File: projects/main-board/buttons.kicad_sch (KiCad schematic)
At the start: 16 parts, among them SW10 SW_Push, SW11 SW_Push, SW12 SW_Push, SW13 SW_Push, SW14 SW_Push, SW15 SW_Push, SW16 SW_Push, SW17 SW_Push, SW2 SW_Push, SW3 SW_Push, SW4 SW_Push, SW5 SW_Push, SW6 SW_Push, SW7 SW_Push, SW8 SW_Push, SW9 SW_Push

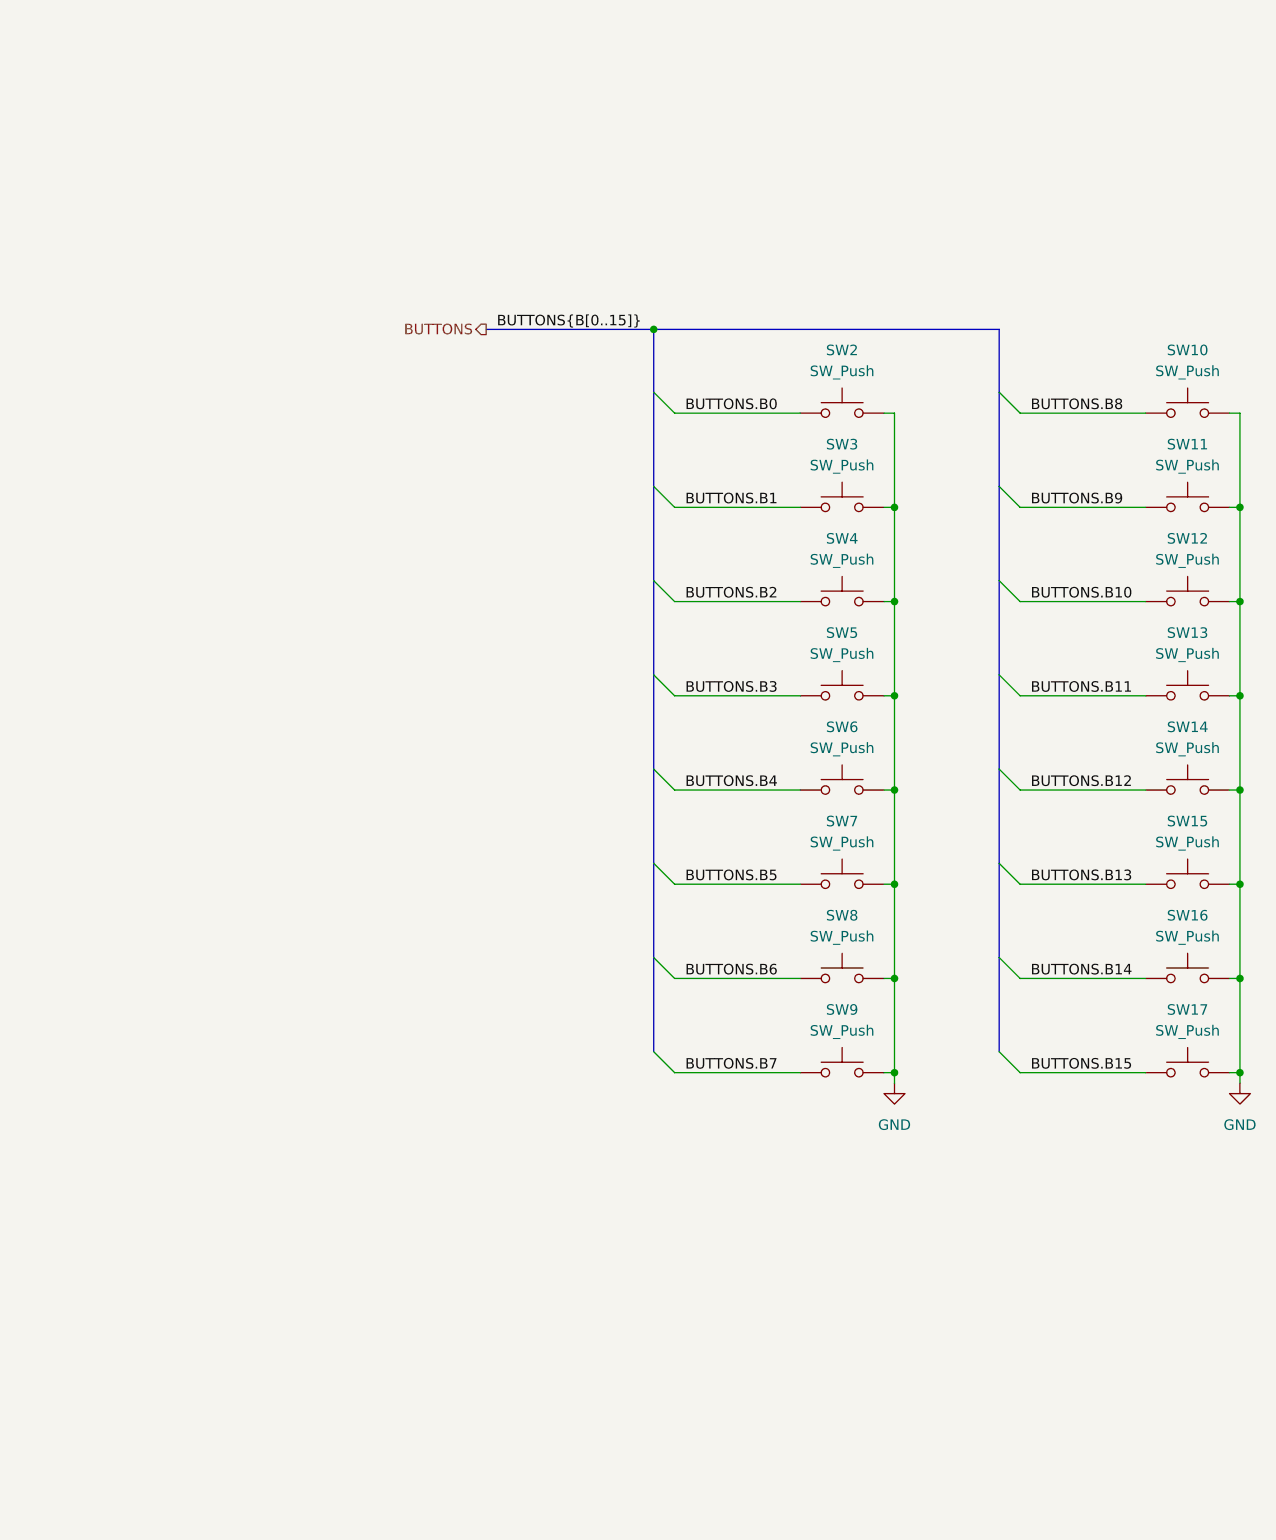
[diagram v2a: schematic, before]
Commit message: Add footprints
- Inductors
- Switches
- Buttons
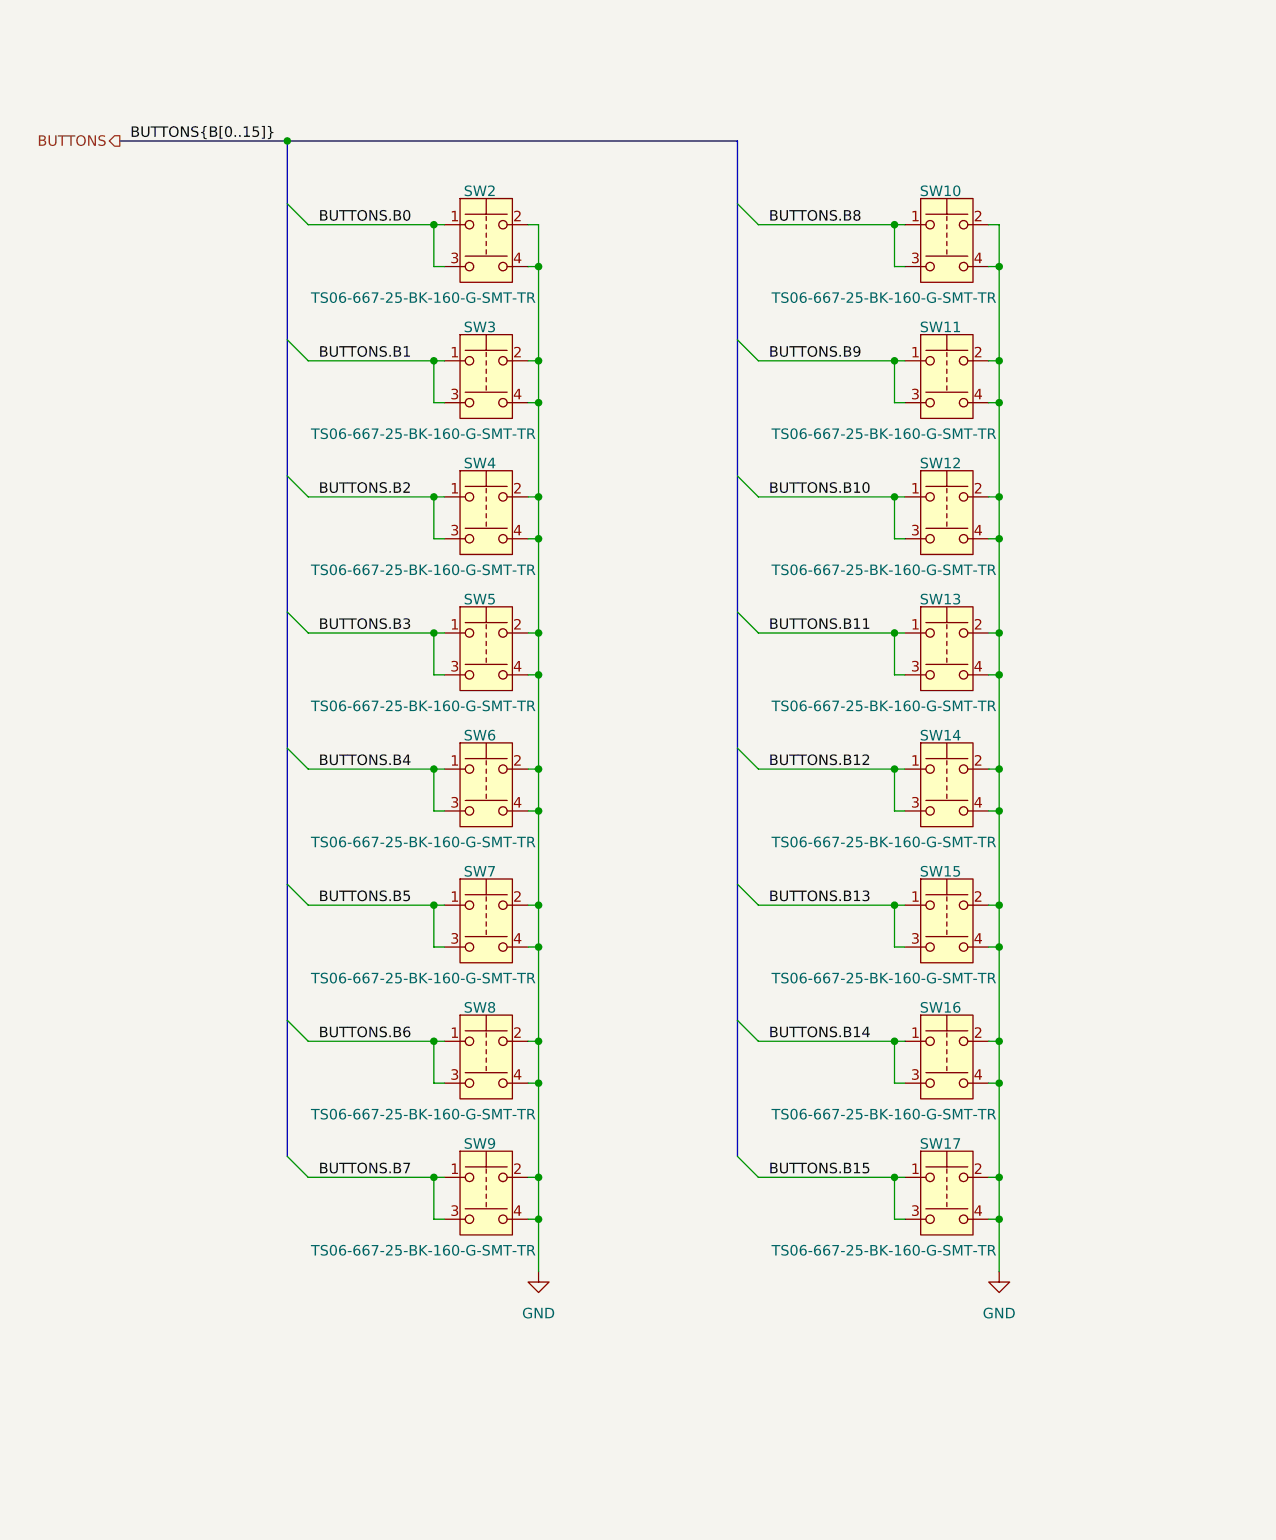
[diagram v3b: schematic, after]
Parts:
- removed SW10, SW11, SW12, SW13, SW14, SW15, SW16, SW17, SW2, SW3, SW4, SW5, SW6, SW7, SW8, SW9: SW_Push, symbol Switch:SW_Push
- added SW10, SW11, SW12, SW13, SW14, SW15, SW16, SW17, SW2, SW3, SW4, SW5, SW6, SW7, SW8, SW9: TS06-667-25-BK-160-G-SMT-TR, footprint-library:TS06-667-25-BK-160-G-SMT-TR, symbol symbol-library:TS06-667-25-BK-160-G-SMT-TR
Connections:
- net BUTTONS.B0: now also SW2.1, SW2.3
- net BUTTONS.B1: now also SW3.1, SW3.3
- net BUTTONS.B10: now also SW12.1, SW12.3
- net BUTTONS.B11: now also SW13.1, SW13.3
- net BUTTONS.B12: now also SW14.1, SW14.3
- net BUTTONS.B13: now also SW15.1, SW15.3
- net BUTTONS.B14: now also SW16.1, SW16.3
- net BUTTONS.B15: now also SW17.1, SW17.3
- net BUTTONS.B2: now also SW4.1, SW4.3
- net BUTTONS.B3: now also SW5.1, SW5.3
- net BUTTONS.B4: now also SW6.1, SW6.3
- net BUTTONS.B5: now also SW7.1, SW7.3
- net BUTTONS.B6: now also SW8.1, SW8.3
- net BUTTONS.B7: now also SW9.1, SW9.3
- net BUTTONS.B8: now also SW10.1, SW10.3
- net BUTTONS.B9: now also SW11.1, SW11.3
- net GND: now also SW10.2, SW10.4, SW11.2, SW11.4, SW12.2, SW12.4, SW13.2, SW13.4, SW14.2, SW14.4, SW15.2, SW15.4, SW16.2, SW16.4, SW17.2, SW17.4, SW2.2, SW2.4, SW3.2, SW3.4, SW4.2, SW4.4, SW5.2, SW5.4, SW6.2, SW6.4, SW7.2, SW7.4, SW8.2, SW8.4, SW9.2, SW9.4

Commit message: Fix footprint DRC errors.
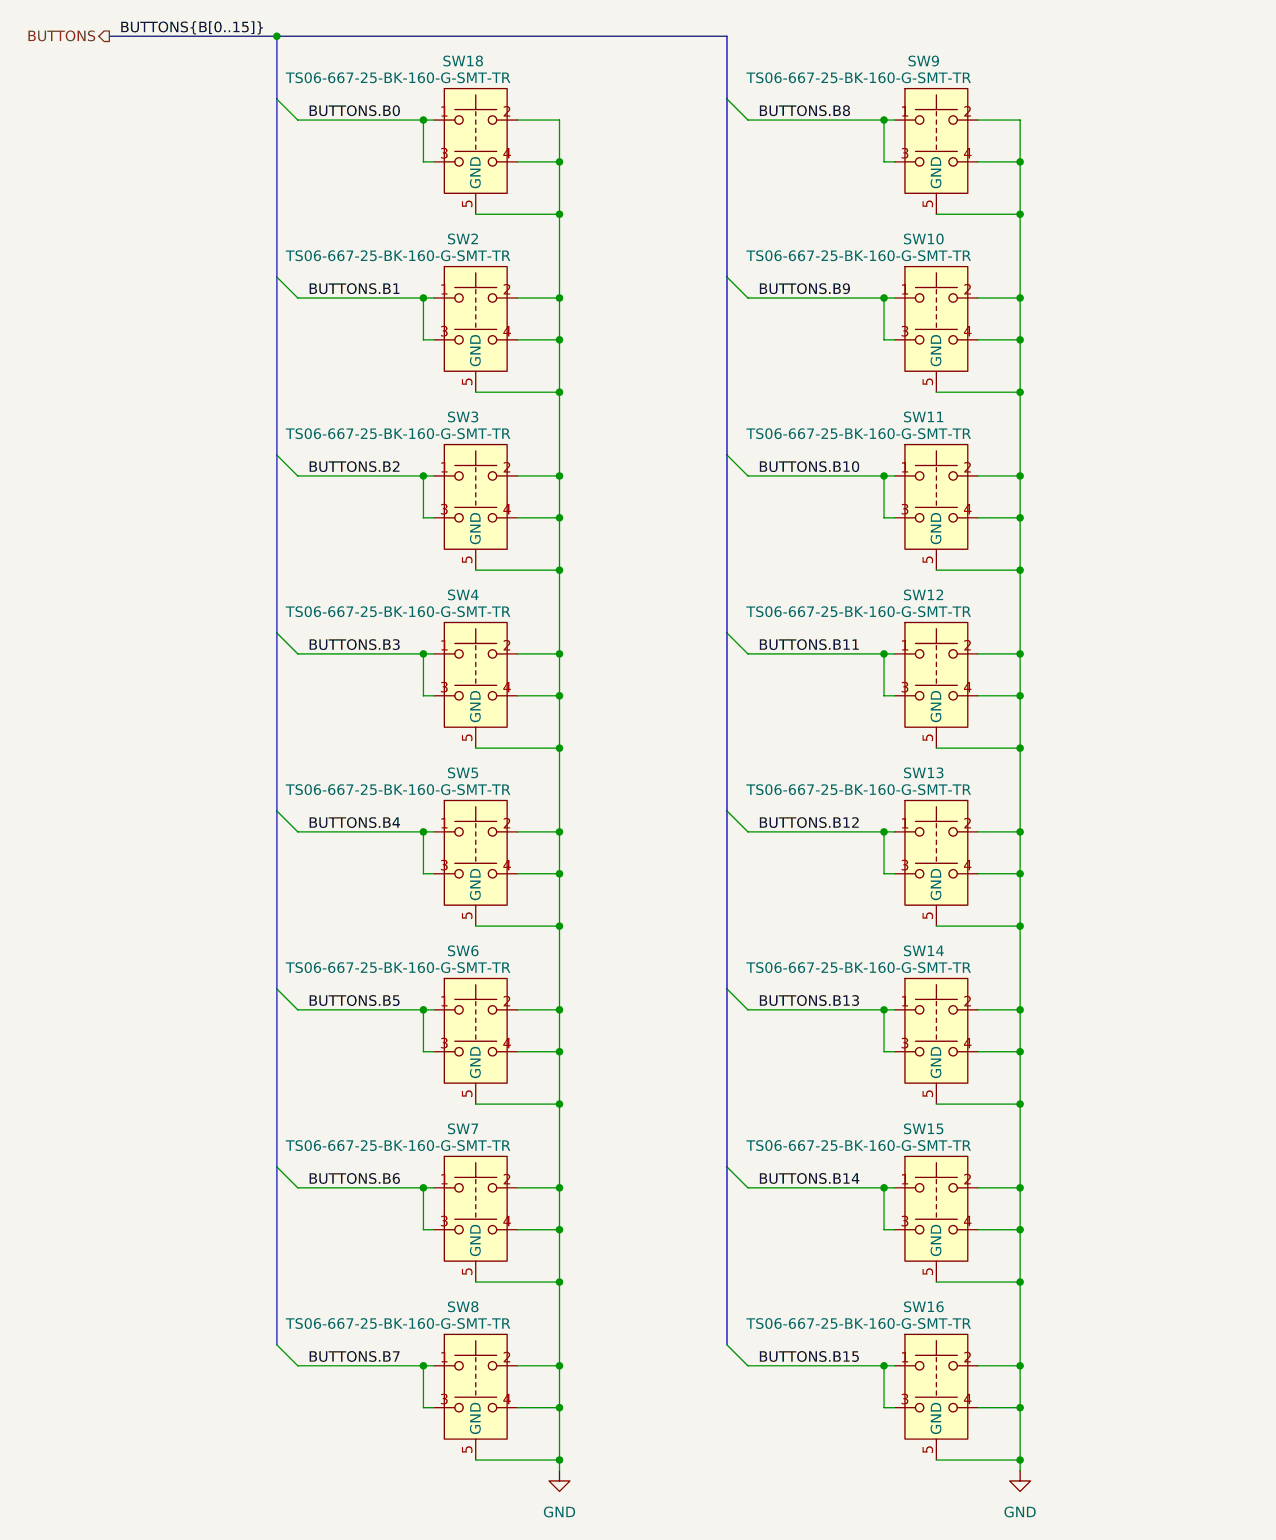
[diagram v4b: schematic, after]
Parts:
- removed SW17: TS06-667-25-BK-160-G-SMT-TR, footprint-library:TS06-667-25-BK-160-G-SMT-TR, symbol symbol-library:TS06-667-25-BK-160-G-SMT-TR
- added SW18: TS06-667-25-BK-160-G-SMT-TR, footprint-library:TS06-667-25-BK-160-G-SMT-TR, symbol symbol-library:TS06-667-25-BK-160-G-SMT-TR
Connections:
- net BUTTONS.B0: now also SW18.1, SW18.3; no longer SW2.1, SW2.3
- net BUTTONS.B1: now also SW2.1, SW2.3; no longer SW3.1, SW3.3
- net BUTTONS.B10: now also SW11.1, SW11.3; no longer SW12.1, SW12.3
- net BUTTONS.B11: now also SW12.1, SW12.3; no longer SW13.1, SW13.3
- net BUTTONS.B12: now also SW13.1, SW13.3; no longer SW14.1, SW14.3
- net BUTTONS.B13: now also SW14.1, SW14.3; no longer SW15.1, SW15.3
- net BUTTONS.B14: now also SW15.1, SW15.3; no longer SW16.1, SW16.3
- net BUTTONS.B15: now also SW16.1, SW16.3
- net BUTTONS.B2: now also SW3.1, SW3.3; no longer SW4.1, SW4.3
- net BUTTONS.B3: now also SW4.1, SW4.3; no longer SW5.1, SW5.3
- net BUTTONS.B4: now also SW5.1, SW5.3; no longer SW6.1, SW6.3
- net BUTTONS.B5: now also SW6.1, SW6.3; no longer SW7.1, SW7.3
- net BUTTONS.B6: now also SW7.1, SW7.3; no longer SW8.1, SW8.3
- net BUTTONS.B7: now also SW8.1, SW8.3; no longer SW9.1, SW9.3
- net BUTTONS.B8: now also SW9.1, SW9.3; no longer SW10.1, SW10.3
- net BUTTONS.B9: now also SW10.1, SW10.3; no longer SW11.1, SW11.3
- net GND: now also SW10.5 (GND), SW11.5 (GND), SW12.5 (GND), SW13.5 (GND), SW14.5 (GND), SW15.5 (GND), SW16.5 (GND), SW2.5 (GND), SW3.5 (GND), SW4.5 (GND), SW5.5 (GND), SW6.5 (GND), SW7.5 (GND), SW8.5 (GND), SW9.5 (GND), SW18.2, SW18.4, SW18.5 (GND)

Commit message: Update render.
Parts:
- removed SW15, SW16, SW7, SW8: TS06-667-25-BK-160-G-SMT-TR, footprint-library:TS06-667-25-BK-160-G-SMT-TR, symbol symbol-library:TS06-667-25-BK-160-G-SMT-TR
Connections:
- net BUTTONS.B12 is gone; now on net BUTTONS.B10: SW13.1, SW13.3
- net BUTTONS.B13 is gone; now on net BUTTONS.B11: SW14.1, SW14.3
- net BUTTONS.B10: no longer SW11.1, SW11.3
- net BUTTONS.B11: no longer SW12.1, SW12.3
- net BUTTONS.B6: now also SW9.1, SW9.3
- net BUTTONS.B7: now also SW10.1, SW10.3
- net BUTTONS.B8: now also SW11.1, SW11.3; no longer SW9.1, SW9.3
- net BUTTONS.B9: now also SW12.1, SW12.3; no longer SW10.1, SW10.3

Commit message: Update render
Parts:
- removed SW13, SW14: TS06-667-25-BK-160-G-SMT-TR, footprint-library:TS06-667-25-BK-160-G-SMT-TR, symbol symbol-library:TS06-667-25-BK-160-G-SMT-TR

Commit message: WIP splitting main board into 3
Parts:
- removed SW10, SW11, SW12, SW18, SW2, SW3, SW4, SW5, SW6, SW9: TS06-667-25-BK-160-G-SMT-TR, footprint-library:TS06-667-25-BK-160-G-SMT-TR, symbol symbol-library:TS06-667-25-BK-160-G-SMT-TR
